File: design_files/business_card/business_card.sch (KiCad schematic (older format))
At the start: 35 parts, among them J1 Conn_01x06, J2 Conn_01x04_Male, SW1 SW_Push, SW2 SW_Push, SW3 SW_Push, SW4 SW_Push, U1 ATTINY85-20SU, U2 TLC5940PWP

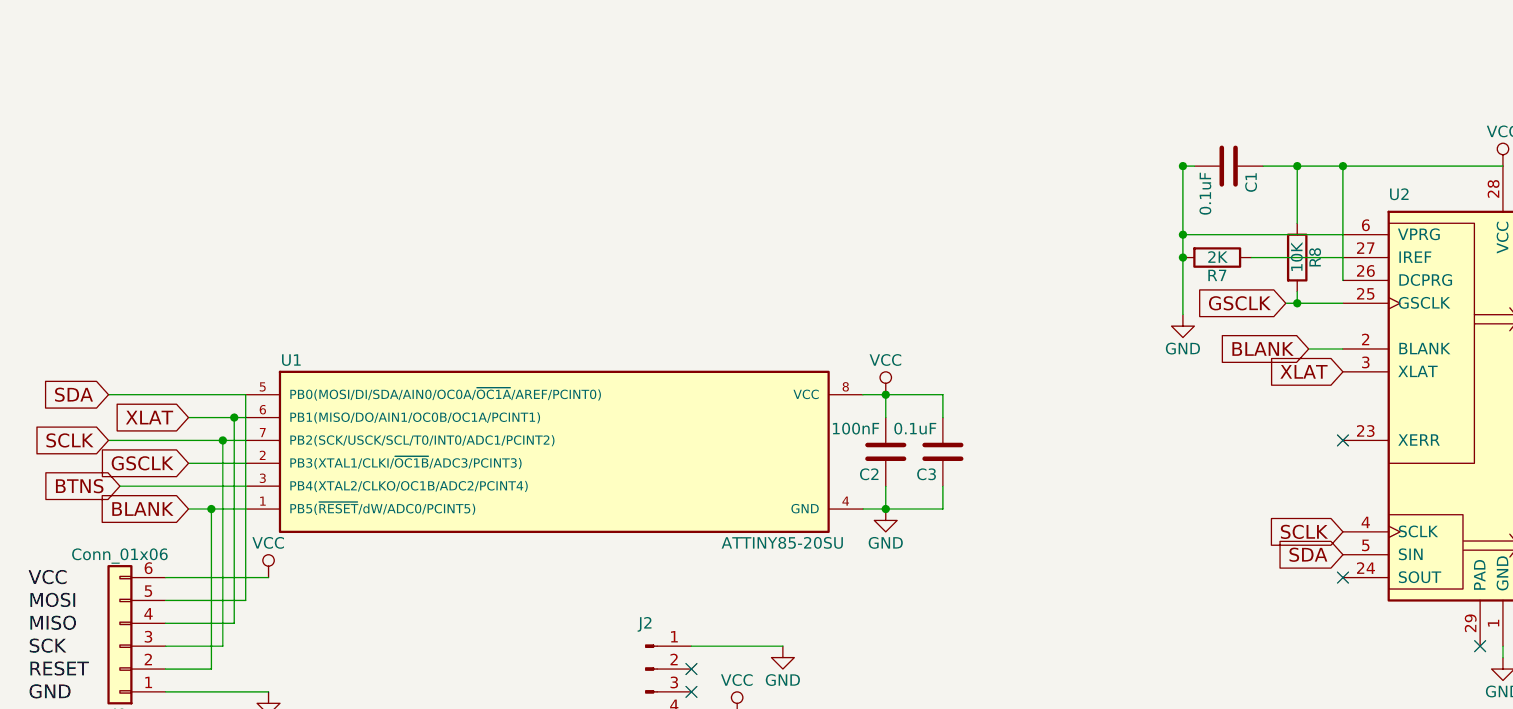
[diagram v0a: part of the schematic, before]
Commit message: switching to 3 wire control
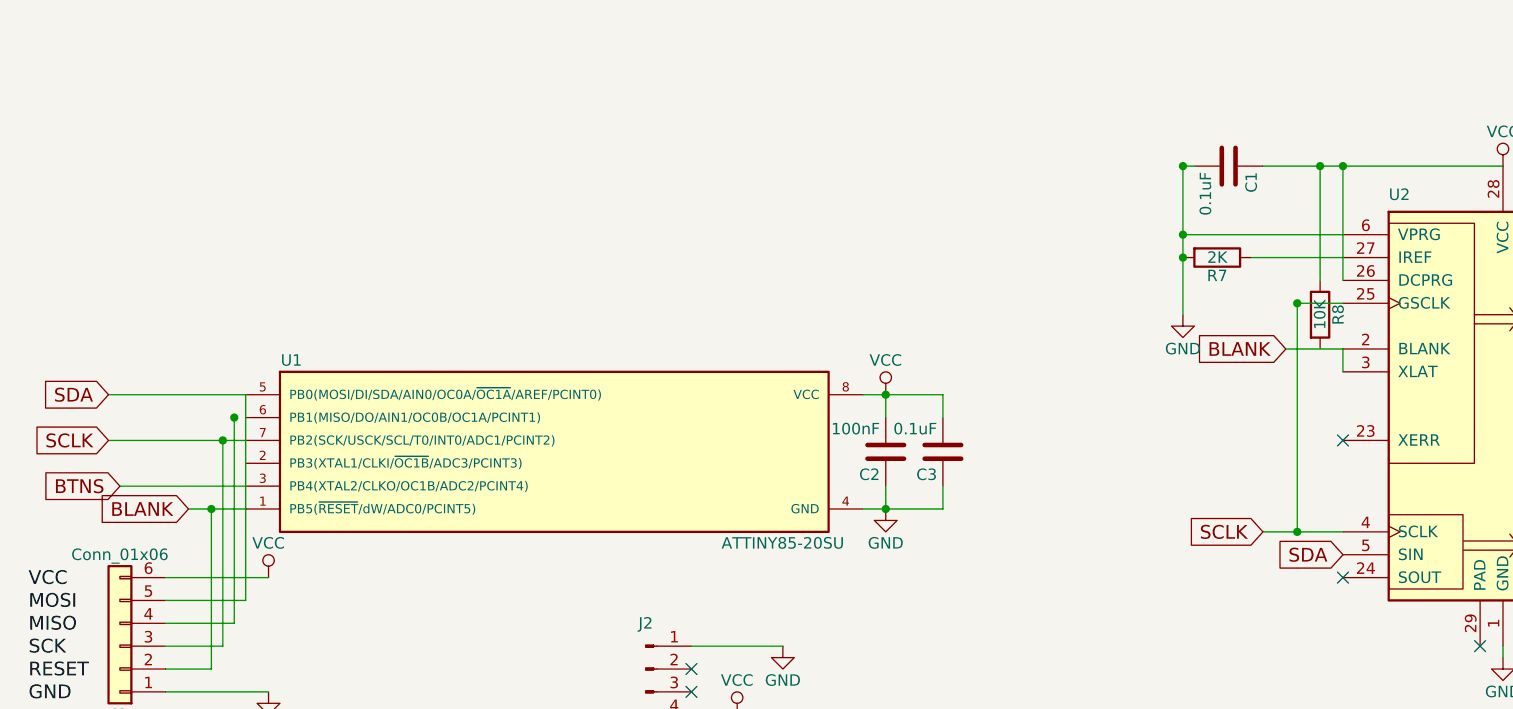
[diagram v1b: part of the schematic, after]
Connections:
- net BLANK: now also U2.3 (XLAT)
- net SCLK: now also U2.25 (GSCLK)
- removed net GSCLK: R8.2, U1.2 (PB3(XTAL1/CLKI/~OC1B~/ADC3/PCINT3)), U2.25 (GSCLK)
- removed net XLAT: J1.4 (Pin_4), U1.6 (PB1(MISO/DO/AIN1/OC0B/OC1A/PCINT1)), U2.3 (XLAT)
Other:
- moved on the sheet: R8
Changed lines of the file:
@@
 	0    1    1    0
 $EndComp
-Text GLabel 6850 4300 0    60   Input ~ 0
+Text GLabel 6500 4300 0    60   Input ~ 0
 SCLK
 Text GLabel 6850 4400 0    60   Input ~ 0
 SDA
-Text GLabel 6850 3600 0    60   Input ~ 0
-XLAT
-Text GLabel 6700 3500 0    60   Input ~ 0
+Text GLabel 6600 3500 0    60   Input ~ 0
 BLANK
-Text GLabel 6600 3300 0    60   Input ~ 0
-GSCLK
 $Comp
 L GND #PWR9
@@
 Text GLabel 1450 3700 0    60   Input ~ 0
 SDA
-Text GLabel 1800 3800 0    60   Input ~ 0
-XLAT
 Text GLabel 1800 4200 0    60   Input ~ 0
 BLANK
-Text GLabel 1800 4000 0    60   Input ~ 0
-GSCLK
 $Comp
 L R R8
 U 1 1 59C5D4C8
-P 6650 3100
-F 0 "R8" V 6730 3100 50  0000 C CNN
-F 1 "10K" V 6650 3100 50  0000 C CNN
-F 2 "Resistors_SMD:R_0805" V 6580 3100 50  0001 C CNN
-F 3 "10K" H 6650 3100 50  0001 C CNN
-	1    6650 3100
+P 6750 3350
+F 0 "R8" V 6830 3350 50  0000 C CNN
+F 1 "10K" V 6750 3350 50  0000 C CNN
+F 2 "Resistors_SMD:R_0805" V 6680 3350 50  0001 C CNN
+F 3 "10K" H 6750 3350 50  0001 C CNN
+	1    6750 3350
 	1    0    0    -1
 $EndComp
@@
 Wire Wire Line
 	2050 3700 1450 3700
-Wire Wire Line
-	6650 2950 6650 2700
-Connection ~ 6650 2700
-Wire Wire Line
-	6650 3300 6650 3250
 Connection ~ 6650 3300
 Wire Wire Line
-	6700 3500 6850 3500
+	6600 3500 6850 3500
 Wire Wire Line
 	2550 6800 2350 6800
@@
 Wire Wire Line
 	6150 2700 6200 2700
-Wire Wire Line
-	6600 3300 6850 3300
 Connection ~ 6150 3100
-Wire Wire Line
-	1800 3800 2050 3800
-Wire Wire Line
-	2050 4000 1800 4000
 Wire Wire Line
 	1500 4100 2050 4100
@@
 	5100 3700 5100 3800
 Connection ~ 4850 3700
+Wire Wire Line
+	6500 4300 6850 4300
+Connection ~ 6650 4300
+Wire Wire Line
+	6650 3300 6850 3300
+Wire Wire Line
+	6850 3500 6850 3600
+Wire Wire Line
+	6650 3300 6650 4300
+Wire Wire Line
+	6750 3200 6750 2700
+Connection ~ 6750 2700
 $EndSCHEMATC

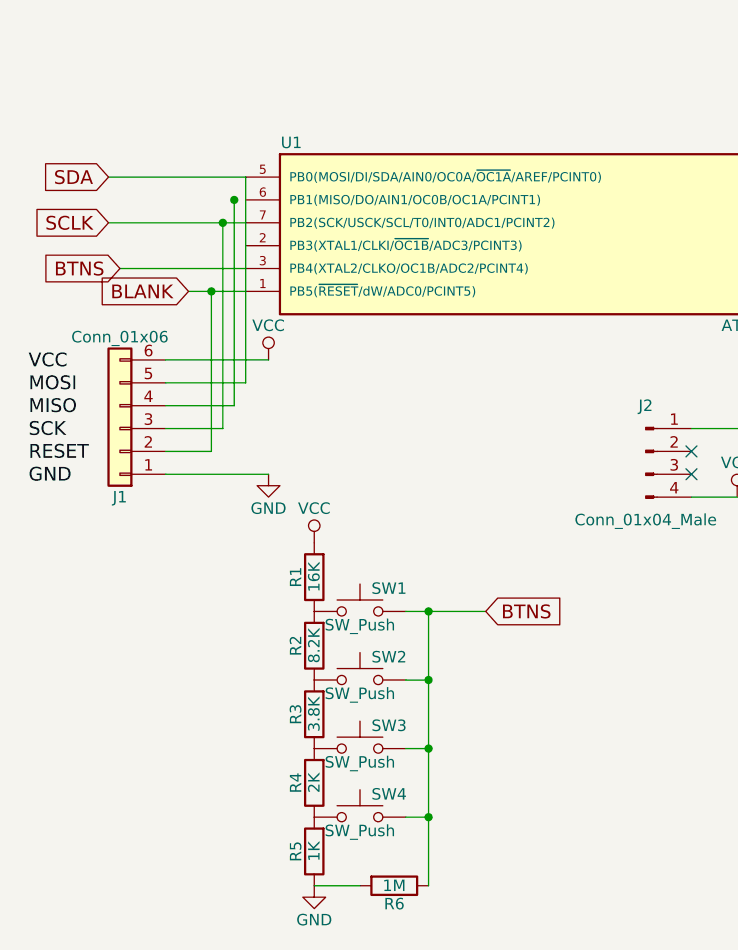
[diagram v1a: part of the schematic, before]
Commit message: 2 buttons and 15 leds
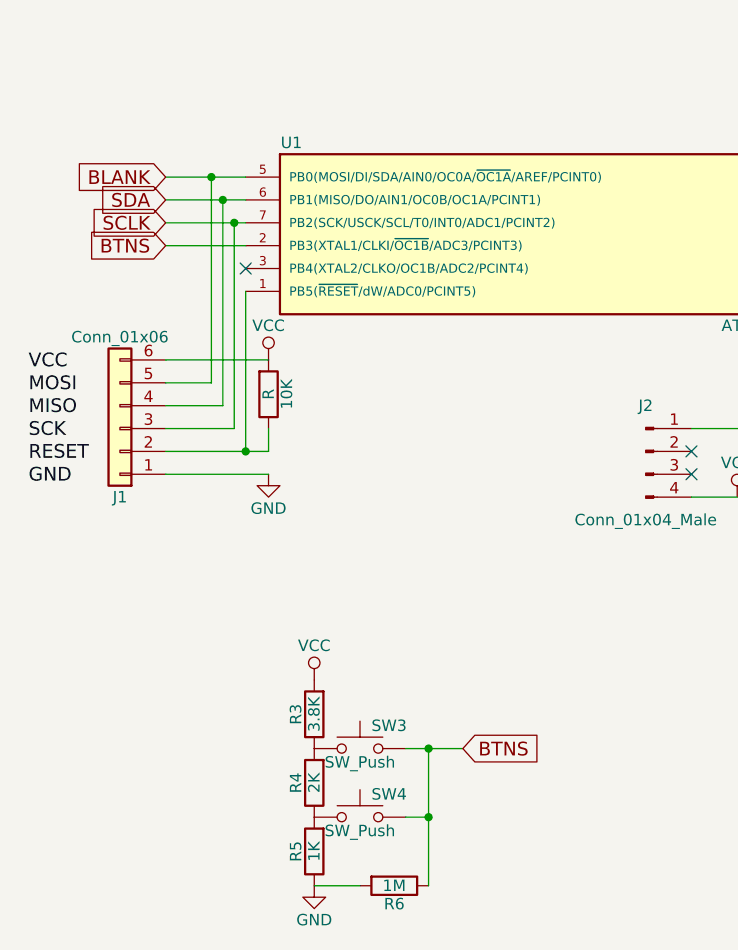
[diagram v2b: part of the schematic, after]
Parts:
- removed R1: 16K, Resistors_SMD:R_0805, symbol R
- removed R2: 8.2K, Resistors_SMD:R_0805, symbol R
- removed SW1, SW2: SW_Push, Buttons_Switches_SMD:SW_SPST_SKQG, symbol SW_Push
- added 10K: R, Resistors_SMD:R_0805, symbol R
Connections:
- net BLANK: now also J1.5 (Pin_5), U1.5 (PB0(MOSI/DI/SDA/AIN0/OC0A/~OC1A~/AREF/PCINT0)); no longer J1.2 (Pin_2), U1.1 (PB5(~RESET~/dW/ADC0/PCINT5))
- net BTNS: now also U1.2 (PB3(XTAL1/CLKI/~OC1B~/ADC3/PCINT3)); no longer U1.3 (PB4(XTAL2/CLKO/OC1B/ADC2/PCINT4))
- net SDA: now also J1.4 (Pin_4), U1.6 (PB1(MISO/DO/AIN1/OC0B/OC1A/PCINT1)); no longer J1.5 (Pin_5), U1.5 (PB0(MOSI/DI/SDA/AIN0/OC0A/~OC1A~/AREF/PCINT0))
- net VCC: now also R3.2, 10K.2
- new net: 10K.1, J1.2 (Pin_2), U1.1 (PB5(~RESET~/dW/ADC0/PCINT5))
- no-connect marks 5 -> 6
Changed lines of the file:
@@
 	0    1    1    0
 $EndComp
-Text GLabel 1450 3900 0    60   Input ~ 0
+Text GLabel 1700 3900 0    60   Input ~ 0
 SCLK
-Text GLabel 1450 3700 0    60   Input ~ 0
+Text GLabel 1700 3800 0    60   Input ~ 0
 SDA
-Text GLabel 1800 4200 0    60   Input ~ 0
+Text GLabel 1700 3700 0    60   Input ~ 0
 BLANK
 $Comp
@@
 F 3 "10K" H 6750 3350 50  0001 C CNN
 	1    6750 3350
-	1    0    0    -1
-$EndComp
-$Comp
-L SW_Push SW1
-U 1 1 59C62029
-P 2550 5600
-F 0 "SW1" H 2600 5700 50  0000 L CNN
-F 1 "SW_Push" H 2550 5540 50  0000 C CNN
-F 2 "Buttons_Switches_SMD:SW_SPST_SKQG" H 2550 5800 50  0001 C CNN
-F 3 "" H 2550 5800 50  0001 C CNN
-	1    2550 5600
-	1    0    0    -1
-$EndComp
-$Comp
-L SW_Push SW2
-U 1 1 59C62455
-P 2550 5900
-F 0 "SW2" H 2600 6000 50  0000 L CNN
-F 1 "SW_Push" H 2550 5840 50  0000 C CNN
-F 2 "Buttons_Switches_SMD:SW_SPST_SKQG" H 2550 6100 50  0001 C CNN
-F 3 "" H 2550 6100 50  0001 C CNN
-	1    2550 5900
-	1    0    0    -1
-$EndComp
-$Comp
-L SW_Push SW3
-U 1 1 59C624D3
-P 2550 6200
-F 0 "SW3" H 2600 6300 50  0000 L CNN
-F 1 "SW_Push" H 2550 6140 50  0000 C CNN
-F 2 "Buttons_Switches_SMD:SW_SPST_SKQG" H 2550 6400 50  0001 C CNN
-F 3 "" H 2550 6400 50  0001 C CNN
-	1    2550 6200
 	1    0    0    -1
 $EndComp
@@
 $EndComp
 $Comp
-L R R3
-U 1 1 59C629B6
-P 2350 6050
-F 0 "R3" V 2430 6050 50  0000 C CNN
-F 1 "3.8K" V 2350 6050 50  0000 C CNN
-F 2 "Resistors_SMD:R_0805" V 2280 6050 50  0001 C CNN
-F 3 "" H 2350 6050 50  0001 C CNN
-	1    2350 6050
-	-1   0    0    1
-$EndComp
-$Comp
-L R R2
-U 1 1 59C62AB0
-P 2350 5750
-F 0 "R2" V 2430 5750 50  0000 C CNN
-F 1 "8.2K" V 2350 5750 50  0000 C CNN
-F 2 "Resistors_SMD:R_0805" V 2280 5750 50  0001 C CNN
-F 3 "" H 2350 5750 50  0001 C CNN
-	1    2350 5750
-	-1   0    0    1
-$EndComp
-$Comp
-L R R1
-U 1 1 59C62B37
-P 2350 5450
-F 0 "R1" V 2430 5450 50  0000 C CNN
-F 1 "16K" V 2350 5450 50  0000 C CNN
-F 2 "Resistors_SMD:R_0805" V 2280 5450 50  0001 C CNN
-F 3 "" H 2350 5450 50  0001 C CNN
-	1    2350 5450
-	-1   0    0    1
-$EndComp
-$Comp
 L R R5
 U 1 1 59C62C0C
@@
 L VCC #PWR3
 U 1 1 59C62D86
-P 2350 5300
-F 0 "#PWR3" H 2350 5150 50  0001 C CNN
-F 1 "VCC" H 2350 5450 50  0000 C CNN
-F 2 "" H 2350 5300 50  0001 C CNN
-F 3 "" H 2350 5300 50  0001 C CNN
-	1    2350 5300
-	1    0    0    -1
-$EndComp
-Text GLabel 1500 4100 0    60   Input ~ 0
+P 2350 5900
+F 0 "#PWR3" H 2350 5750 50  0001 C CNN
+F 1 "VCC" H 2350 6050 50  0000 C CNN
+F 2 "" H 2350 5900 50  0001 C CNN
+F 3 "" H 2350 5900 50  0001 C CNN
+	1    2350 5900
+	1    0    0    -1
+$EndComp
+Text GLabel 1700 4000 0    60   Input ~ 0
 BTNS
-Text GLabel 3100 5600 2    60   Input ~ 0
+Text GLabel 3000 6200 2    60   Input ~ 0
 BTNS
 NoConn ~ 7450 4800
@@
 $EndComp
 $Comp
-L GND #PWR2
-U 1 1 59C6C12B
-P 2150 5000
-F 0 "#PWR2" H 2150 4750 50  0001 C CNN
-F 1 "GND" H 2150 4850 50  0000 C CNN
-F 2 "" H 2150 5000 50  0001 C CNN
-F 3 "" H 2150 5000 50  0001 C CNN
-	1    2150 5000
-	1    0    0    -1
-$EndComp
-$Comp
 L Conn_01x04_Male J2
 U 1 1 59C7247C
@@
 	1    0    0    -1
 $EndComp
+$Comp
+L Conn_01x06 J1
+U 1 1 59C6B0AE
+P 1500 4800
+F 0 "J1" H 1500 5100 50  0000 C CNN
+F 1 "Conn_01x06" H 1500 4400 50  0000 C CNN
+F 2 "pogo_connector:pogo_connector" H 1500 4800 50  0001 C CNN
+F 3 "" H 1500 4800 50  0001 C CNN
+	1    1500 4800
+	-1   0    0    1
+$EndComp
+NoConn ~ 4000 4900
+NoConn ~ 4000 5000
+$Comp
+L VCC #PWR5
+U 1 1 59C7428C
+P 4200 5100
+F 0 "#PWR5" H 4200 4950 50  0001 C CNN
+F 1 "VCC" H 4200 5250 50  0000 C CNN
+F 2 "" H 4200 5100 50  0001 C CNN
+F 3 "" H 4200 5100 50  0001 C CNN
+	1    4200 5100
+	1    0    0    -1
+$EndComp
+$Comp
+L GND #PWR6
+U 1 1 59C7439F
+P 4400 4800
+F 0 "#PWR6" H 4400 4550 50  0001 C CNN
+F 1 "GND" H 4400 4650 50  0000 C CNN
+F 2 "" H 4400 4800 50  0001 C CNN
+F 3 "" H 4400 4800 50  0001 C CNN
+	1    4400 4800
+	1    0    0    -1
+$EndComp
+$Comp
+L VCC #PWR7
+U 1 1 59C54A1F
+P 4850 3700
+F 0 "#PWR7" H 4850 3550 50  0001 C CNN
+F 1 "VCC" H 4850 3850 50  0000 C CNN
+F 2 "" H 4850 3700 50  0001 C CNN
+F 3 "" H 4850 3700 50  0001 C CNN
+	1    4850 3700
+	1    0    0    -1
+$EndComp
+$Comp
+L C C3
+U 1 1 59C56136
+P 5100 3950
+F 0 "C3" H 5125 4050 50  0000 L CNN
+F 1 "0.1uF" H 5125 3850 50  0000 L CNN
+F 2 "Capacitors_SMD:C_0805" H 5138 3800 50  0001 C CNN
+F 3 "" H 5100 3950 50  0001 C CNN
+	1    5100 3950
+	-1   0    0    1
+$EndComp
 Wire Wire Line
 	9850 6350 9850 600
@@
 Connection ~ 6150 3000
 Connection ~ 6150 2700
-Wire Wire Line
-	1450 3900 2050 3900
-Wire Wire Line
-	2050 3700 1450 3700
 Connection ~ 6650 3300
 Wire Wire Line
@@
 	2550 6800 2350 6800
 Wire Wire Line
-	2850 6800 2850 5600
-Wire Wire Line
-	2750 5600 3100 5600
-Wire Wire Line
-	2750 5900 2850 5900
-Connection ~ 2850 5900
-Wire Wire Line
-	2750 6200 2850 6200
+	2750 6200 3000 6200
 Connection ~ 2850 6200
 Wire Wire Line
 	2750 6500 2850 6500
 Connection ~ 2850 6500
-Connection ~ 2850 5600
 Connection ~ 9850 1000
 Connection ~ 9850 1400
@@
 Connection ~ 6150 3100
 Wire Wire Line
-	1500 4100 2050 4100
-Wire Wire Line
-	2050 4200 1800 4200
-Wire Wire Line
-	1700 4600 2050 4600
-Wire Wire Line
-	2050 4600 2050 3700
-Wire Wire Line
-	1700 4700 2000 4700
-Wire Wire Line
-	2000 4700 2000 3800
-Connection ~ 2000 3800
-Wire Wire Line
-	1700 4800 1950 4800
-Wire Wire Line
-	1950 4800 1950 3900
-Connection ~ 1950 3900
-Wire Wire Line
-	1700 4900 1900 4900
-Wire Wire Line
-	1900 4900 1900 4200
-Connection ~ 1900 4200
-Wire Wire Line
-	2150 5000 1700 5000
-Wire Wire Line
-	1700 4500 2150 4500
-$Comp
-L Conn_01x06 J1
-U 1 1 59C6B0AE
-P 1500 4800
-F 0 "J1" H 1500 5100 50  0000 C CNN
-F 1 "Conn_01x06" H 1500 4400 50  0000 C CNN
-F 2 "pogo_connector:pogo_connector" H 1500 4800 50  0001 C CNN
-F 3 "" H 1500 4800 50  0001 C CNN
-	1    1500 4800
-	-1   0    0    1
-$EndComp
-NoConn ~ 4000 4900
-NoConn ~ 4000 5000
-$Comp
-L VCC #PWR5
-U 1 1 59C7428C
-P 4200 5100
-F 0 "#PWR5" H 4200 4950 50  0001 C CNN
-F 1 "VCC" H 4200 5250 50  0000 C CNN
-F 2 "" H 4200 5100 50  0001 C CNN
-F 3 "" H 4200 5100 50  0001 C CNN
-	1    4200 5100
-	1    0    0    -1
-$EndComp
-Wire Wire Line
 	4000 5100 4200 5100
-$Comp
-L GND #PWR6
-U 1 1 59C7439F
-P 4400 4800
-F 0 "#PWR6" H 4400 4550 50  0001 C CNN
-F 1 "GND" H 4400 4650 50  0000 C CNN
-F 2 "" H 4400 4800 50  0001 C CNN
-F 3 "" H 4400 4800 50  0001 C CNN
-	1    4400 4800
-	1    0    0    -1
-$EndComp
 Wire Wire Line
 	4400 4800 4000 4800
-$Comp
-L VCC #PWR7
-U 1 1 59C54A1F
-P 4850 3700
-F 0 "#PWR7" H 4850 3550 50  0001 C CNN
-F 1 "VCC" H 4850 3850 50  0000 C CNN
-F 2 "" H 4850 3700 50  0001 C CNN
-F 3 "" H 4850 3700 50  0001 C CNN
-	1    4850 3700
-	1    0    0    -1
-$EndComp
-$Comp
-L C C3
-U 1 1 59C56136
-P 5100 3950
-F 0 "C3" H 5125 4050 50  0000 L CNN
-F 1 "0.1uF" H 5125 3850 50  0000 L CNN
-F 2 "Capacitors_SMD:C_0805" H 5138 3800 50  0001 C CNN
-F 3 "" H 5100 3950 50  0001 C CNN
-	1    5100 3950
-	-1   0    0    1
-$EndComp
 Wire Wire Line
 	5100 4200 5100 4100
@@
 	6750 3200 6750 2700
 Connection ~ 6750 2700
+Wire Wire Line
+	2150 4500 1700 4500
+$Comp
+L GND #PWR?
+U 1 1 59EAB901
+P 2150 5000
+F 0 "#PWR?" H 2150 4750 50  0001 C CNN
+F 1 "GND" H 2150 4850 50  0000 C CNN
+F 2 "" H 2150 5000 50  0001 C CNN
+F 3 "" H 2150 5000 50  0001 C CNN
+	1    2150 5000
+	1    0    0    -1
+$EndComp
+Wire Wire Line
+	2150 5000 1700 5000
+Wire Wire Line
+	2050 4200 2050 4900
+Wire Wire Line
+	1700 4900 2150 4900
+Wire Wire Line
+	1700 4800 2000 4800
+Wire Wire Line
+	2000 4800 2000 3900
+Wire Wire Line
+	1700 3900 2050 3900
+Wire Wire Line
+	1700 4700 1950 4700
+Wire Wire Line
+	1950 4700 1950 3800
+Wire Wire Line
+	1700 3800 2050 3800
+Wire Wire Line
+	1700 4600 1900 4600
+Wire Wire Line
+	1900 4600 1900 3700
+Wire Wire Line
+	1700 3700 2050 3700
+Wire Wire Line
+	2050 4000 1700 4000
+Connection ~ 2000 3900
+Connection ~ 1950 3800
+Connection ~ 1900 3700
+$Comp
+L R 10K
+U 1 1 59EAD6BF
+P 2150 4650
+F 0 "10K" V 2230 4650 50  0000 C CNN
+F 1 "R" V 2150 4650 50  0000 C CNN
+F 2 "Resistors_SMD:R_0805" V 2080 4650 50  0001 C CNN
+F 3 "" H 2150 4650 50  0001 C CNN
+	1    2150 4650
+	1    0    0    1
+$EndComp
+NoConn ~ 2050 4100
+Wire Wire Line
+	2150 4900 2150 4800
+Connection ~ 2050 4900
+$Comp
+L R R3
+U 1 1 59C629B6
+P 2350 6050
+F 0 "R3" V 2430 6050 50  0000 C CNN
+F 1 "3.8K" V 2350 6050 50  0000 C CNN
+F 2 "Resistors_SMD:R_0805" V 2280 6050 50  0001 C CNN
+F 3 "" H 2350 6050 50  0001 C CNN
+	1    2350 6050
+	-1   0    0    1
+$EndComp
+$Comp
+L SW_Push SW3
+U 1 1 59C624D3
+P 2550 6200
+F 0 "SW3" H 2600 6300 50  0000 L CNN
+F 1 "SW_Push" H 2550 6140 50  0000 C CNN
+F 2 "Buttons_Switches_SMD:SW_SPST_SKQG" H 2550 6400 50  0001 C CNN
+F 3 "" H 2550 6400 50  0001 C CNN
+	1    2550 6200
+	1    0    0    -1
+$EndComp
+Wire Wire Line
+	2850 6200 2850 6800
 $EndSCHEMATC
